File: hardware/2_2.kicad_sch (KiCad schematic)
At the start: 10 parts, among them U4 KH-TYPE-C-16P, U6 CH572D, U8 HX_JN1_27-2X5P_ZZ_H4_9, X2 XTM20032000DT00351001

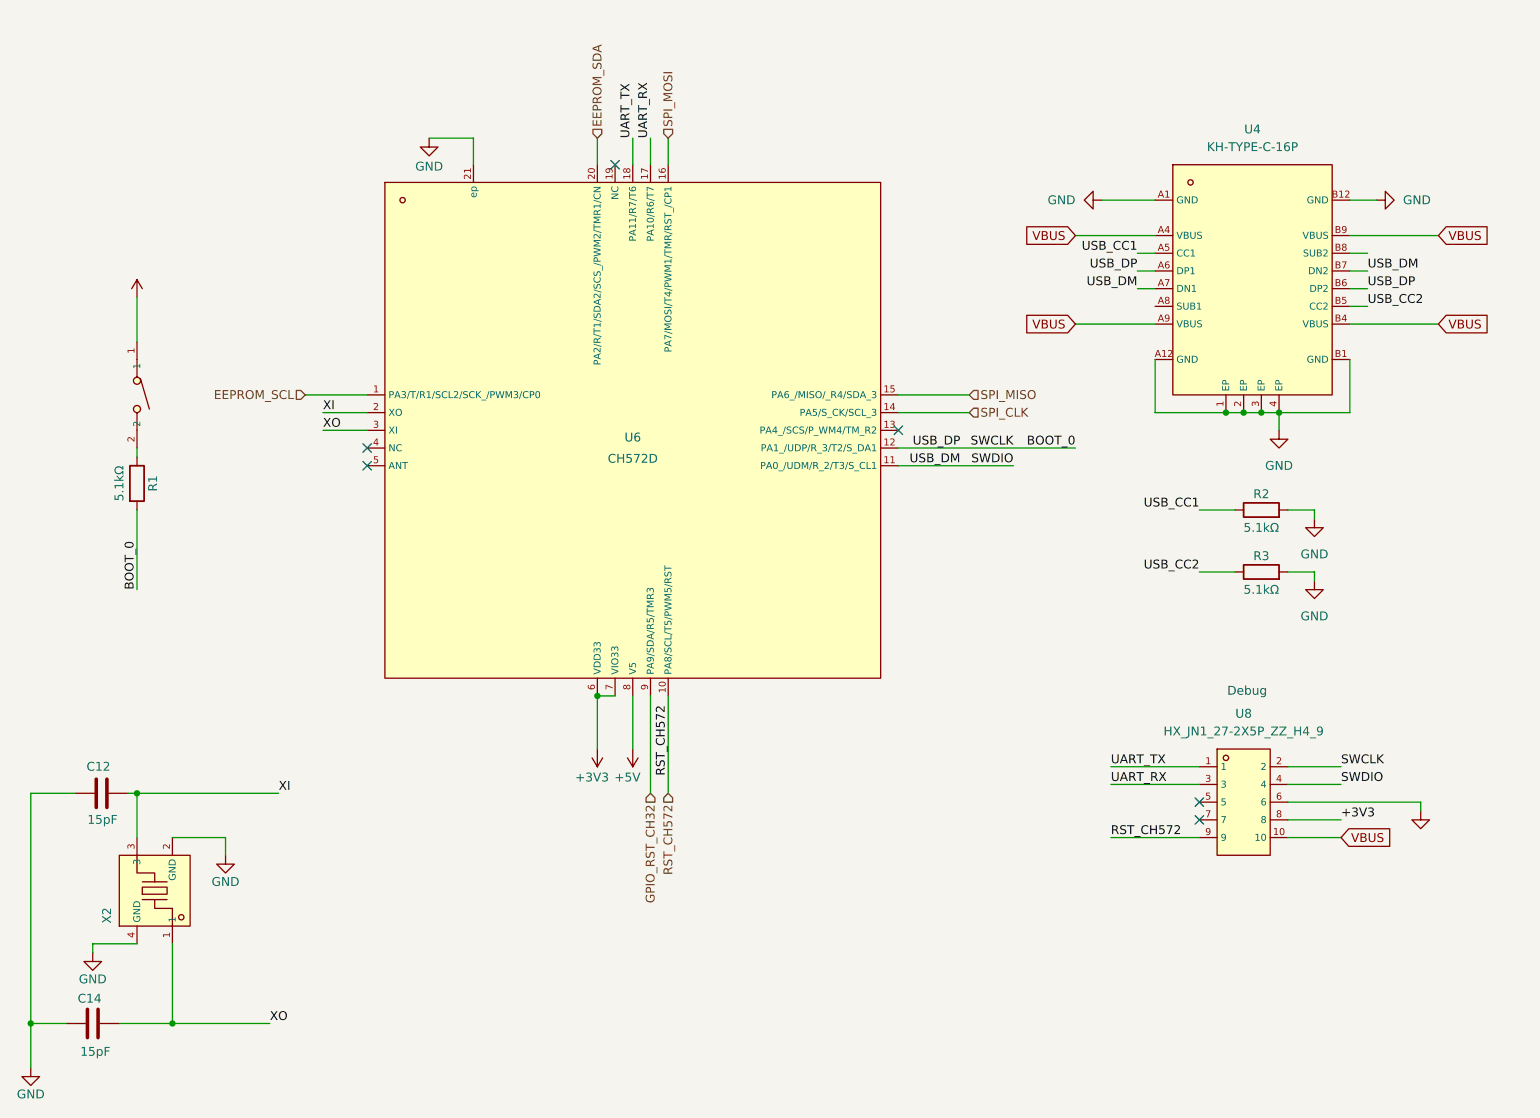
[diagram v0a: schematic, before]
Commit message: refactor: minor schematic visual changes
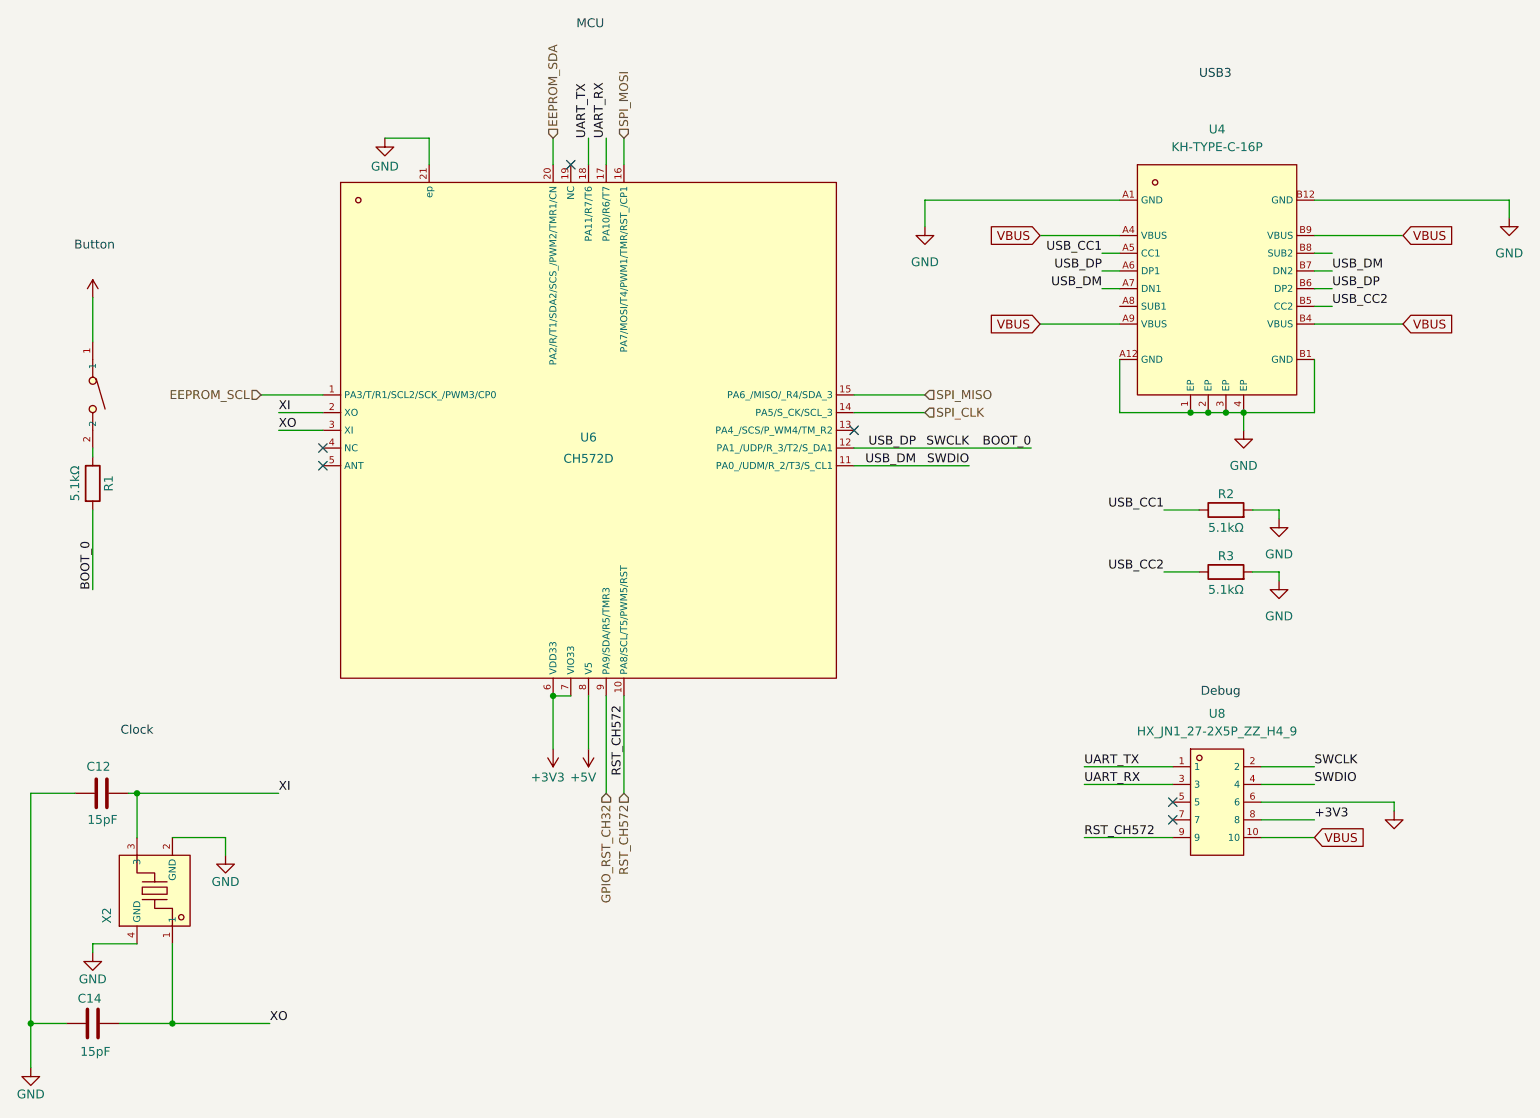
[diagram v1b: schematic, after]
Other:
- note added: "Button"
- note added: "Clock"
- note added: "MCU"
- note added: "USB3"
- moved on the sheet: R1, R2, R3, U4, U6, U8

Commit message: fix: add missing cs line to spi bus
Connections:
- net SPI_CS: now reaches U6.13 (PA4_/SCS/P_WM4/TM_R2)
- no-connect marks 6 -> 5
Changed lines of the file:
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@@
-	)
-	(no_connect
-		(at 140.97 76.2)
 	)
 	(no_connect
@@
 		(pts
 			(xy 102.87 34.29) (xy 102.87 38.1)
+		)
+		(stroke
+			(width 0)
+			(type default)
+		)
+	)
+	(wire
+		(pts
+			(xy 140.97 76.2) (xy 151.13 76.2)
 		)
 		(stroke
@@
 		(effects
 			(font
+				(size 1.27 1.27)
+			)
+			(justify left)
+		)
+	)
+	(hierarchical_label "SPI_CS"
+		(shape input)
+		(at 151.13 76.2 0)
+		(effects
+			(font
